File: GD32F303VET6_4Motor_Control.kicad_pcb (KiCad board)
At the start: 4 copper layers, 100 x 60 mm, 126 parts, among them CN1 KF128L-5.08-2P, CN2 WJ15EDGRC-3.81-2P, CN4 WJ15EDGRC-3.81-2P, J1 TYPE-C-31-M-31, J2 TYPE-C 16PIN 2MD(073), Q1 CJ3134K KF, Q2 CJ3134K KF, SW1 SKRPACE010, U1 XL1509-5.0, U10 SIT3485ESA, U11 TXS0104EPWR, U12 TXS0104EPWR, U13 CH340E, U14 TPD4S012DRYR, U2 B0503S-2WR3L, U3 SY8089A1AAC, U4 CH213K, U5 SY8089AAC, U6 GD32F303VCT6, U7 ISO1050DWR, U9 π131U30, Y1 TAXM8M4RDBCCT2T, Y2 XKXGI-SUA-32.768K

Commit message: 重命名为GD32F303VET6四电机驱动控制板
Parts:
- U6: value GD32F303VCT6 -> GD32F303VET6; footprint kicad_api_lib:GD32F303VCT6 -> kicad_api_lib:GD32F303VET6

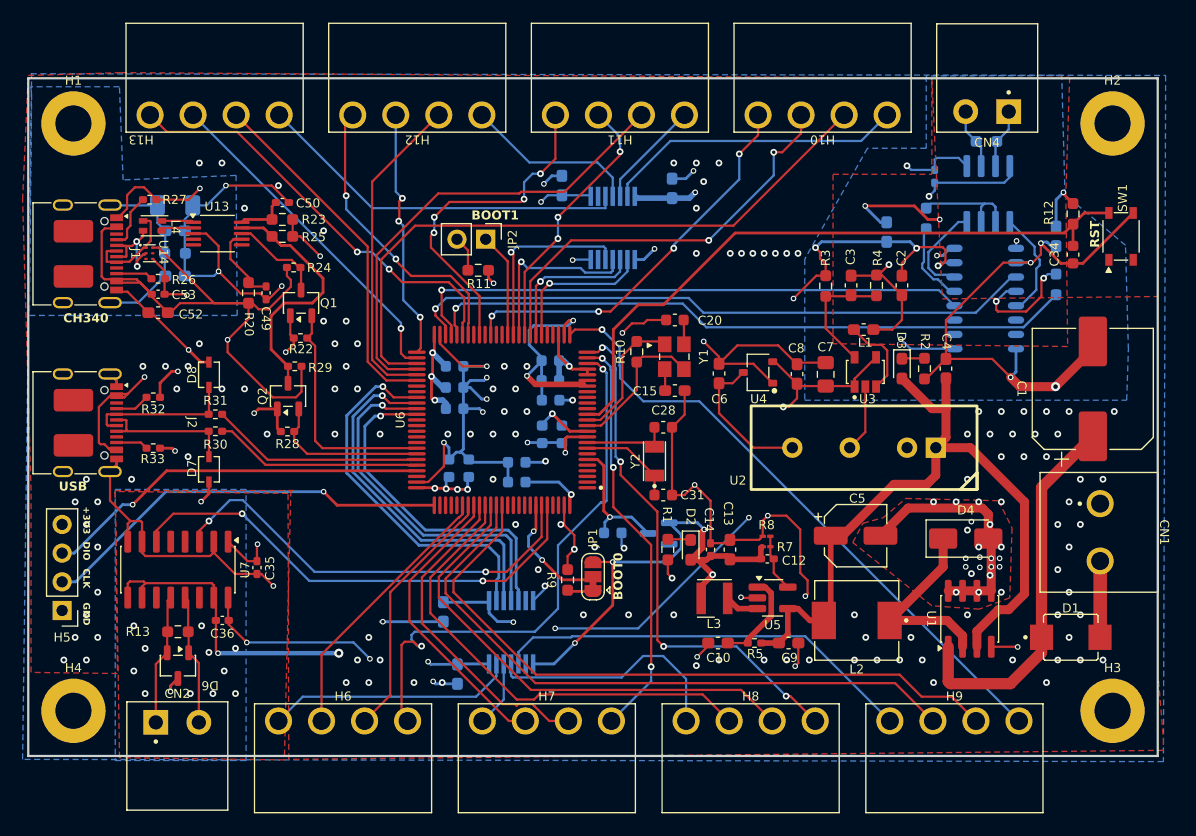
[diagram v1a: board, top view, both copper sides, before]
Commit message: 更新六层控制板设计及嘉立创生产文件
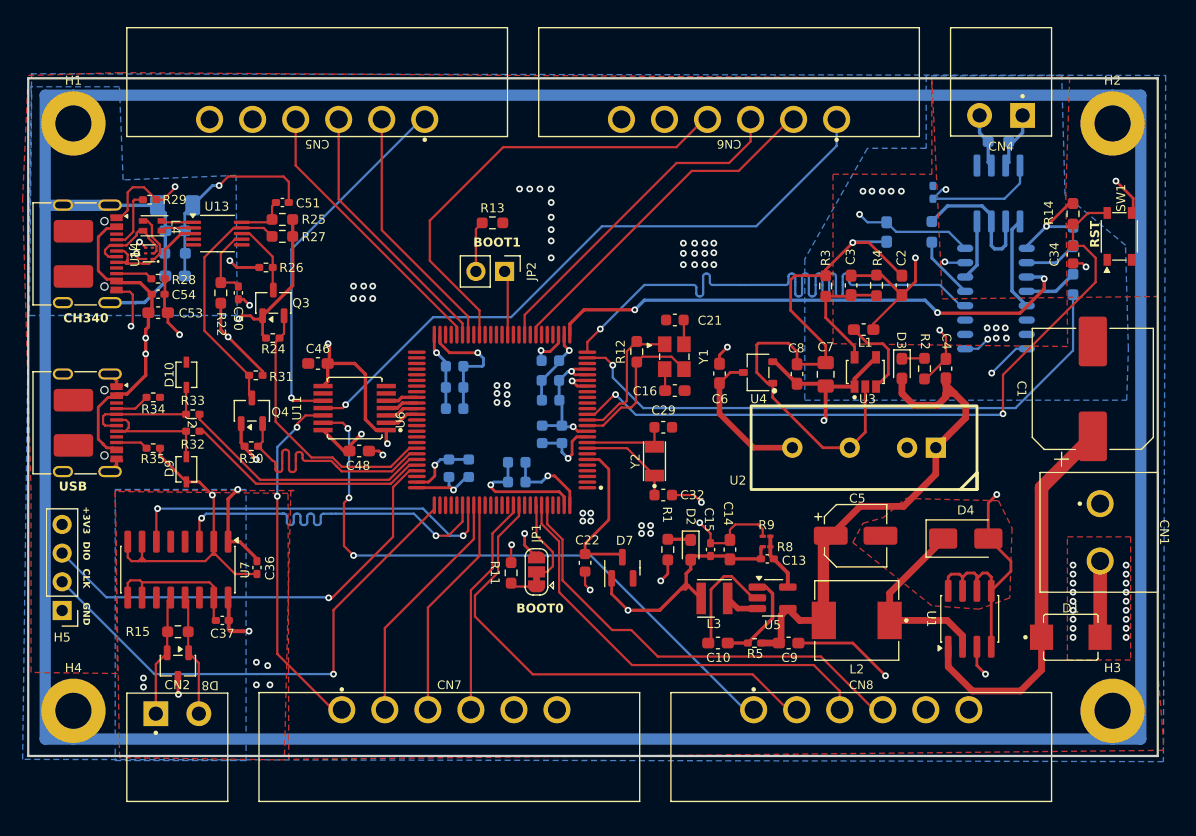
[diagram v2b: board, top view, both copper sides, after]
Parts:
- removed the C46 at (132.8, 68.5)
- removed the C48 at (142.5, 68.8)
- removed H10, H11, H12, H13, H6, H7, H8, H9: KF2EDGRM-3.81-4P, kicad_api_lib:KF2EDGRM-3.81-4P
- removed Q2: CJ3134K KF, Package_TO_SOT_SMD:SOT-23-3
- removed the R28 at (108.5, 90.3)
- removed the R29 at (109.1, 84.5)
- removed U12: TXS0104EPWR, kicad_api_lib:TXS0104EPWR
- added CN5: KF2EDGRM-3.81-6P, kicad_api_lib:KF2EDGRM-3.81-6P, F.Cu at (111.1, 62.6)
- added CN6: KF2EDGRM-3.81-6P, kicad_api_lib:KF2EDGRM-3.81-6P, F.Cu at (147.5, 62.6)
- added CN7: KF2EDGRM-3.81-6P, kicad_api_lib:KF2EDGRM-3.81-6P, F.Cu at (122.8, 114.9)
- added CN8: KF2EDGRM-3.81-6P, kicad_api_lib:KF2EDGRM-3.81-6P, F.Cu at (159.2, 114.9)
- added Q4: CJ3134K KF, Package_TO_SOT_SMD:SOT-23-3, F.Cu at (105.3, 88.4)
- added R30: 4.7K, Resistor_SMD:R_0402_1005Metric_Pad0.72x0.64mm_HandSolder, F.Cu at (105.2, 91.6)
- added R31: 4.7K, Resistor_SMD:R_0402_1005Metric_Pad0.72x0.64mm_HandSolder, F.Cu at (105.6, 85.3)
- C22: renamed from C21; moved to F.Cu
- C46: renamed from C45; moved to F.Cu
- C48: renamed from C47; moved to F.Cu
- D7: renamed from D5; moved to F.Cu
- U11: moved to F.Cu
- moved C46 24.6 mm to (111.2, 84.2), turned to 180 degrees
- moved U11 24.2 mm to (114.4, 88.2), turned to 90 degrees
- moved C48 21.6 mm to (114.8, 92.0), turned to 0 degrees
- moved R11 5.04 mm to (128.2, 102.8)
- moved JP1 5.02 mm to (130.5, 102.7)
- moved D7 4.42 mm to (138.1, 102.3), turned to 90 degrees
- moved R13 4.39 mm to (126.6, 71.8)
- moved C22 3.61 mm to (134.8, 101.9), turned to -90 degrees
- moved JP2 3.31 mm to (127.7, 76.1)
- moved C50 2.45 mm to (104.1, 78.0)
- moved Q3 2.45 mm to (107.2, 78.9)
- moved R22 2.45 mm to (102.5, 78.0)
- moved R24 2.45 mm to (107.2, 82.0)
- moved R26 2.45 mm to (106.5, 75.8)
- moved D10 2.00 mm to (99.5, 85.2)
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- renumbered C12 to C13, C13 to C14, C14 to C15, C15 to C16, C16 to C17, C17 to C18, C18 to C19, C19 to C20, C20 to C21, C22 to C23, C23 to C24, C24 to C25, C25 to C26, C26 to C27, C27 to C28, C28 to C29, C29 to C30, C30 to C31, C31 to C32, C34 to C35, C35 to C36, C36 to C37, C42 to C43, C43 to C44, C44 to C45, C49 to C50, C50 to C51, C51 to C52, C52 to C53, C53 to C54, D8 to D10, D6 to D8, D7 to D9, Q1 to Q3, R9 to R11, R10 to R12, R11 to R13, R12 to R14, R13 to R15, R16 to R18, R17 to R19, R18 to R20, R20 to R22, R22 to R24, R23 to R25, R24 to R26, R25 to R27, R26 to R28, R27 to R29, R30 to R32, R31 to R33, R32 to R34, R33 to R35, R7 to R8, R8 to R9
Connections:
- U11 pad 10: /MCU_Core/Motor_Comm/PWM1_5V_4 -> /MCU_Core/Motor_Comm/PWM1_5V_1
- U11 pad 11: /MCU_Core/Motor_Comm/PWM1_5V_3 -> /MCU_Core/Motor_Comm/PWM1_5V_2
- U11 pad 12: /MCU_Core/Motor_Comm/PWM1_5V_2 -> /MCU_Core/Motor_Comm/PWM1_5V_3
- U11 pad 13: /MCU_Core/Motor_Comm/PWM1_5V_1 -> /MCU_Core/Motor_Comm/PWM1_5V_4
- U11 pad 2: /MCU_Core/PWM1_1 -> /MCU_Core/PWM1_4
- U11 pad 3: /MCU_Core/PWM1_2 -> /MCU_Core/PWM1_3
- U11 pad 4: /MCU_Core/PWM1_3 -> /MCU_Core/PWM1_2
- U11 pad 5: /MCU_Core/PWM1_4 -> /MCU_Core/PWM1_1
- U6 pad 1: unconnected-(U6E-PE2-Pad1) -> (no net)
- U6 pad 2: unconnected-(U6E-PE3-Pad2) -> (no net)
- U6 pad 23: /MCU_Core/FG1_1 -> (no net)
- U6 pad 24: /MCU_Core/FG1_2 -> /MCU_Core/RS485_DE
- U6 pad 25: /MCU_Core/FG1_3 -> /MCU_Core/RS485_TX
- U6 pad 26: /MCU_Core/FG1_4 -> /MCU_Core/RS485_RX
- U6 pad 29: unconnected-(U6E-PA4-Pad29) -> (no net)
- U6 pad 3: unconnected-(U6E-PE4-Pad3) -> (no net)
- U6 pad 30: unconnected-(U6E-PA5-Pad30) -> (no net)
- U6 pad 31: /MCU_Core/PWM2_1 -> (no net)
- U6 pad 32: /MCU_Core/PWM2_2 -> /MCU_Core/BRAKE1_2
- U6 pad 33: /MCU_Core/DIR2_1 -> (no net)
- U6 pad 34: /MCU_Core/DIR2_2 -> /MCU_Core/DIR1_2
- U6 pad 35: /MCU_Core/PWM2_3 -> (no net)
- U6 pad 36: /MCU_Core/PWM2_4 -> (no net)
- U6 pad 38: unconnected-(U6E-PE7-Pad38) -> (no net)
- U6 pad 39: unconnected-(U6E-PE8-Pad39) -> (no net)
- U6 pad 4: unconnected-(U6E-PE5-Pad4) -> (no net)
- U6 pad 40: /MCU_Core/FG2_1 -> (no net)
- U6 pad 41: unconnected-(U6E-PE10-Pad41) -> (no net)
- U6 pad 42: /MCU_Core/FG2_2 -> /MCU_Core/FG1_2
- U6 pad 43: unconnected-(U6E-PE12-Pad43) -> (no net)
- U6 pad 44: /MCU_Core/FG2_3 -> /MCU_Core/BRAKE1_1
- U6 pad 45: /MCU_Core/FG2_4 -> /MCU_Core/FG1_1
- U6 pad 46: /MCU_Core/RS485_DE -> /MCU_Core/DIR1_1
- U6 pad 47: /MCU_Core/RS485_TX -> (no net)
- U6 pad 48: /MCU_Core/RS485_RX -> (no net)
- U6 pad 5: unconnected-(U6E-PE6-Pad5) -> (no net)
- U6 pad 51: /MCU_Core/DIR2_3 -> (no net)
- U6 pad 52: /MCU_Core/DIR2_4 -> (no net)
- U6 pad 53: /MCU_Core/BRAKE2_1 -> (no net)
- U6 pad 54: /MCU_Core/BRAKE2_2 -> (no net)
- U6 pad 55: /MCU_Core/BRAKE2_3 -> (no net)
- U6 pad 56: /MCU_Core/BRAKE2_4 -> (no net)
- U6 pad 57: unconnected-(U6E-PD10-Pad57) -> (no net)
- U6 pad 58: unconnected-(U6E-PD11-Pad58) -> (no net)
- U6 pad 63: unconnected-(U6C-DIR3-Pad63) -> (no net)
- U6 pad 64: unconnected-(U6C-DIR4-Pad64) -> (no net)
- U6 pad 65: unconnected-(U6E-PC8-Pad65) -> (no net)
- U6 pad 66: unconnected-(U6E-PC9-Pad66) -> (no net)
- U6 pad 67: unconnected-(U6E-PA8-Pad67) -> (no net)
- U6 pad 7: unconnected-(U6E-PC13-Pad7) -> (no net)
- U6 pad 73: unconnected-(U6E-NC-Pad73) -> (no net)
- U6 pad 77: unconnected-(U6E-PA15-Pad77) -> (no net)
- U6 pad 80: unconnected-(U6E-PC12-Pad80) -> (no net)
- U6 pad 81: /MCU_Core/BRAKE1_1 -> /MCU_Core/CAN_RX
- U6 pad 82: /MCU_Core/DIR1_1 -> /MCU_Core/CAN_TX
- U6 pad 83: /MCU_Core/BRAKE1_2 -> /MCU_Core/BRAKE1_3
- U6 pad 84: /MCU_Core/DIR1_2 -> /MCU_Core/DIR1_3
- U6 pad 85: /MCU_Core/BRAKE1_3 -> (no net)
- U6 pad 86: /MCU_Core/DIR1_3 -> (no net)
- U6 pad 87: /MCU_Core/BRAKE1_4 -> (no net)
- U6 pad 88: /MCU_Core/DIR1_4 -> (no net)
- U6 pad 89: unconnected-(U6E-PB3-Pad89) -> (no net)
- U6 pad 90: unconnected-(U6E-PB4-Pad90) -> /MCU_Core/FG1_3
- U6 pad 91: unconnected-(U6E-PB5-Pad91) -> /MCU_Core/BRAKE1_4
- U6 pad 92: unconnected-(U6E-PB6-Pad92) -> (no net)
- U6 pad 93: unconnected-(U6E-PB7-Pad93) -> (no net)
- U6 pad 95: /MCU_Core/CAN_RX -> /MCU_Core/DIR1_4
- U6 pad 96: /MCU_Core/CAN_TX -> /MCU_Core/FG1_4
- U6 pad 97: unconnected-(U6E-PE0-Pad97) -> (no net)
- U6 pad 98: unconnected-(U6E-PE1-Pad98) -> (no net)
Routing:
- net GND: track 301.2 -> 203.2 mm, vias 180 -> 65
- net +5V: track 155.4 -> 94.2 mm, vias 4 -> 7
- net Earth: track 280.1 -> 340.7 mm
- net /MCU_Core/BRAKE2_1: track 58.3 -> 0.00 mm
- net /MCU_Core/Motor_Comm/PWM1_5V_2: track 5.84 -> 57.8 mm, vias 0 -> 1
- net /MCU_Core/BRAKE2_2: track 41.6 -> 0.00 mm
- net /MCU_Core/FG2_4: track 37.9 -> 0.00 mm, vias 2 -> 0
- net /MCU_Core/DIR2_1: track 37.0 -> 0.00 mm, vias 2 -> 0
- net /MCU_Core/FG2_1: track 35.3 -> 0.00 mm, vias 4 -> 0
- net /MCU_Core/Motor_Comm/PWM2_5V_4: track 33.4 -> 0.00 mm
- net /MCU_Core/BRAKE2_4: track 31.7 -> 0.00 mm
- net /MCU_Core/PWM1_1: track 33.3 -> 2.82 mm, vias 1 -> 0
- net /MCU_Core/DIR2_4: track 30.3 -> 0.00 mm, vias 1 -> 0
- net /MCU_Core/FG2_2: track 30.0 -> 0.00 mm, vias 4 -> 0
- net /MCU_Core/PWM1_2: track 32.6 -> 2.89 mm, vias 1 -> 0
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- added copper zone on F.Cu, net +24V
- added copper zone on In3.Cu, net +24V
- added copper zone on In4.Cu, net GND
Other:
- copper layers 4 -> 6

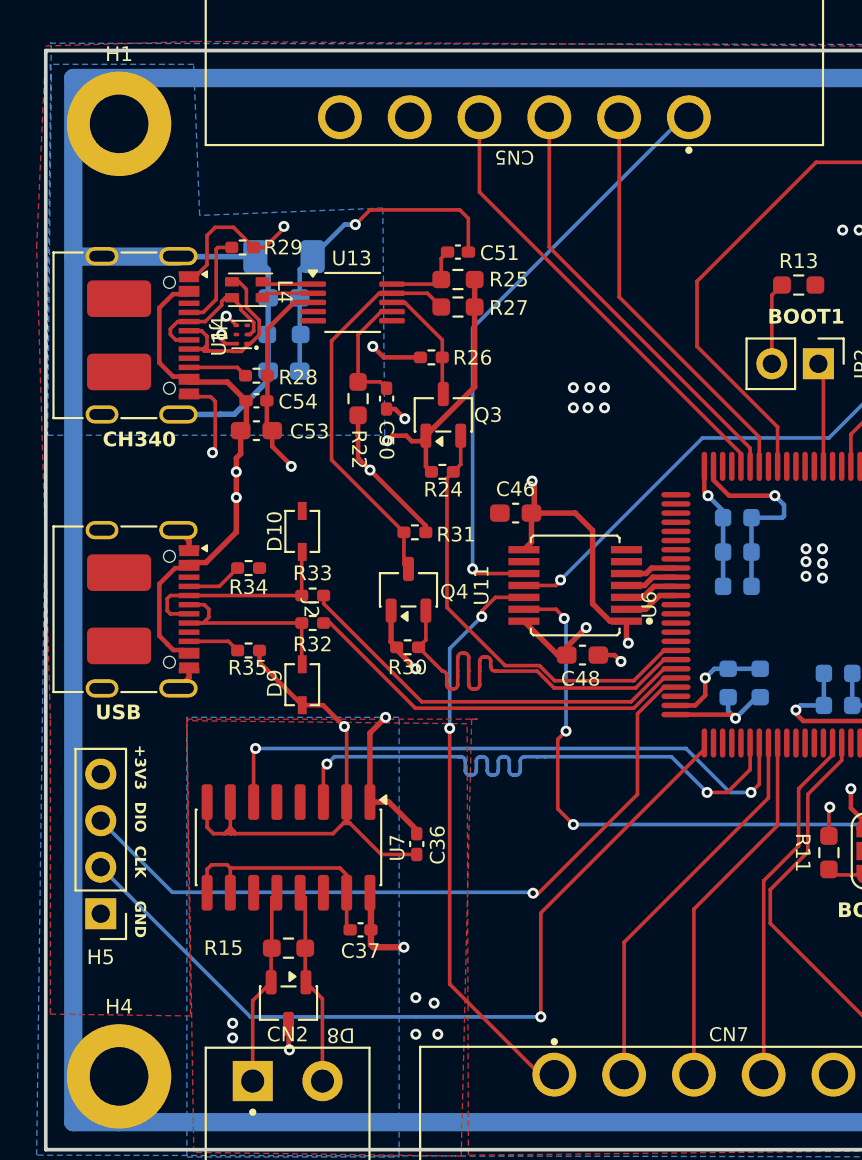
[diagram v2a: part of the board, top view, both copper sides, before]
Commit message: 更新电机控制板原理图与PCB设计
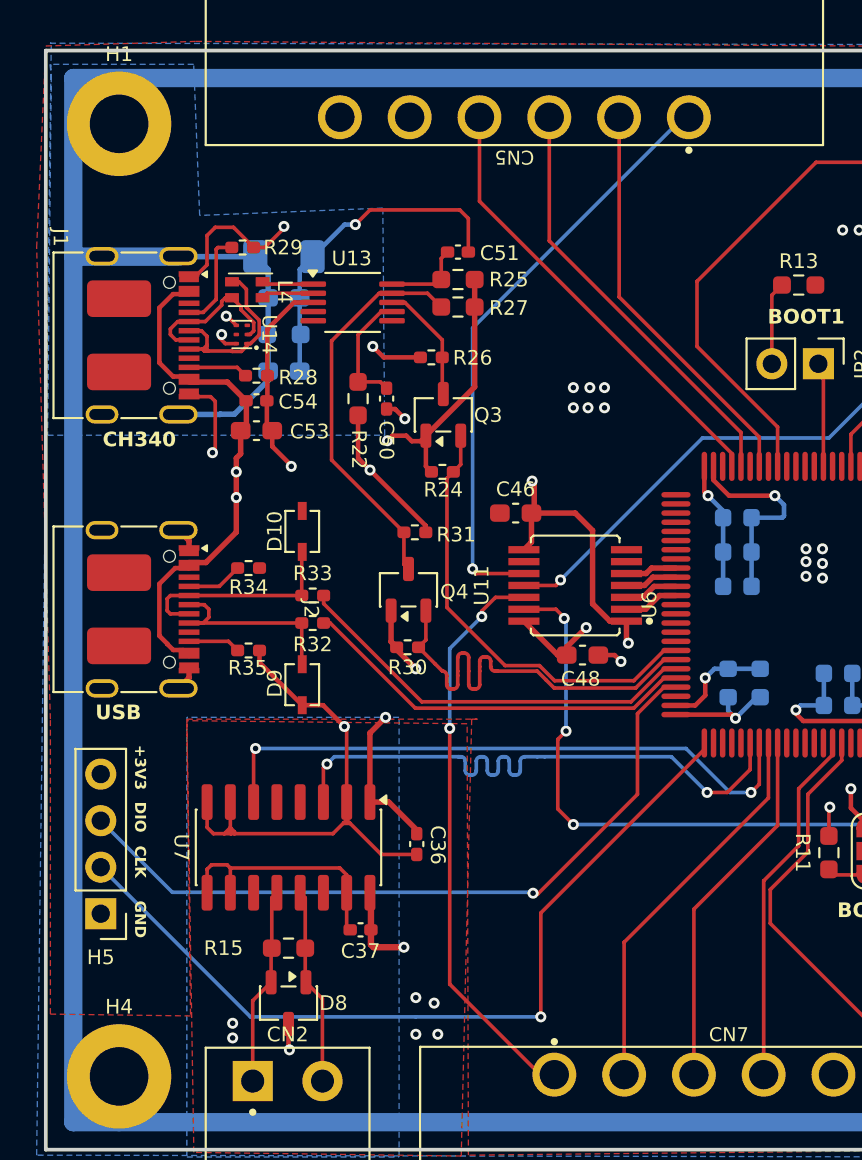
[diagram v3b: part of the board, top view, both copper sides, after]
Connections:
- CN5 pad 3: /MCU_Core/FG1_1 -> /MCU_Core/DIR1_1
- CN5 pad 4: /MCU_Core/DIR1_1 -> /MCU_Core/FG1_1
- U6 pad 45: /MCU_Core/FG1_1 -> (no net)
- U6 pad 47: (no net) -> /MCU_Core/FG1_1
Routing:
- net /MCU_Core/DIR1_1: track 25.3 -> 23.4 mm
- net /MCU_Core/FG1_1: track 23.9 -> 24.8 mm
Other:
- board text added: "BRAKE1_1"
- board text added: "BRAKE1_2"
- board text added: "BRAKE1_3"
- board text added: "BRAKE1_4"
- board text removed: "BRK1_1"
- board text removed: "BRK1_2"
- board text removed: "BRK1_3"
- board text removed: "BRK1_4"
- board text removed: "BRK2_1"
- board text removed: "BRK2_2"
- board text removed: "BRK2_3"
- board text removed: "BRK2_4"
- board text removed: "DIR2_1"
- board text removed: "DIR2_2"
- board text removed: "DIR2_3"
- board text removed: "DIR2_4"
- board text removed: "FG2_1"
- board text removed: "FG2_2"
- board text removed: "FG2_3"
- board text removed: "FG2_4"
- board text removed: "PWM2_1"
- board text removed: "PWM2_2"
- board text removed: "PWM2_3"
- board text removed: "PWM2_4"

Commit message: 更新PCB布局与铺铜设计
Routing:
- net GNDS: track 118.2 -> 75.5 mm, vias 22 -> 33
- net GND: track 203.2 -> 206.1 mm, vias 65 -> 102
- removed copper zone on In1.Cu, net GND
